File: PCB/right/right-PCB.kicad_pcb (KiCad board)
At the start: 2 copper layers, 171 x 95 mm, 55 parts, among them J1 Modulo-Jack, J2 Modulo-Jack, SW1 SW_Push, SW10 SW_Push, SW11 SW_Push, SW12 SW_Push, SW13 SW_Push, SW14 SW_Push, SW15 SW_Push, SW16 SW_Push, SW17 SW_Push, SW18 SW_Push, SW19 SW_Push, SW2 SW_Push, SW20 SW_Push, SW21 SW_Push, SW22 SW_Push, SW23 SW_Push, SW24 SW_Push, SW25 SW_Push, SW26 SW_Push, SW27 SW_Push, SW28 SW_Push, SW29 SW_Push, SW3 SW_Push, SW30 SW_Push, SW31 SW_Push, SW32 SW_Push, SW33 SW_Push, SW34 SW_Push, SW35 SW_Push, SW36 SW_Push, SW37 SW_Push, SW38 SW_Push, SW4 SW_Push, SW5 SW_Push, SW50 SW_DIP_x04, SW6 SW_Push, SW7 SW_Push, SW8 SW_Push, SW9 SW_Push, U1 MCP23017_SP, U2 MCP23017_SP, U3 MCP23017_SP

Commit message: add sign
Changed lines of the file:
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@@
     (pad "" np_thru_hole circle (at 2.54 -5.08) (size 3 3) (drill 3) (layers *.Cu *.Mask))
   )
-  (gr_text "satsuma JP SMD rev.1          Designed by @ysni_pub" (at 102.235 137.16) (layer B.SilkS)
-    (effects (font (size 2 2) (thickness 0.2)) (justify mirror))
+  (gr_text "satsuma JP SMD rev.1    Designed by @ysni_pub" (at 179.07 137.795) (layer F.SilkS)
+    (effects (font (size 1.5 1.5) (thickness 0.15)))
   )
   (gr_circle (center 71.275 102.15) (end 71.755 104.14) (layer Dwgs.User) (width 0.15))

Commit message: add silk
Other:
- board text added: "1MΩ"
- board text added: "1μF"
- board text added: "A2"
- board text added: "KHS42E"
- board text added: "LED"
- board text added: "MCP23017-E/SO"
- board text added: "OFF"
- board text added: "ON"
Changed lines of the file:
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@@
   (general
     (thickness 1.6)
-    (drawings 25)
+    (drawings 35)
     (tracks 610)
     (zones 0)
@@
     (pad "" np_thru_hole circle (at 2.54 -5.08) (size 3 3) (drill 3) (layers *.Cu *.Mask))
   )
+  (gr_text MCP23017-E/SO (at 166.37 102.235) (layer B.SilkS)
+    (effects (font (size 1 1) (thickness 0.15)) (justify mirror))
+  )
+  (gr_text MCP23017-E/SO (at 161.29 64.135) (layer B.SilkS)
+    (effects (font (size 1 1) (thickness 0.15)) (justify mirror))
+  )
+  (gr_text MCP23017-E/SO (at 109.22 102.235) (layer B.SilkS)
+    (effects (font (size 1 1) (thickness 0.15)) (justify mirror))
+  )
+  (gr_text LED (at 83.185 104.775) (layer F.SilkS)
+    (effects (font (size 1 1) (thickness 0.15)))
+  )
+  (gr_text 1MΩ (at 90.805 66.675) (layer F.SilkS)
+    (effects (font (size 1 1) (thickness 0.15)))
+  )
+  (gr_text 1μF (at 104.775 66.04) (layer B.SilkS)
+    (effects (font (size 1 1) (thickness 0.15)) (justify mirror))
+  )
+  (gr_text A2 (at 76.835 59.055) (layer B.SilkS)
+    (effects (font (size 1 1) (thickness 0.15)) (justify mirror))
+  )
+  (gr_text OFF (at 79.375 68.58) (layer B.SilkS)
+    (effects (font (size 1 1) (thickness 0.15)) (justify mirror))
+  )
+  (gr_text ON (at 78.74 60.96) (layer B.SilkS)
+    (effects (font (size 1 1) (thickness 0.15)) (justify mirror))
+  )
+  (gr_text KHS42E (at 74.93 64.77) (layer B.SilkS)
+    (effects (font (size 1 1) (thickness 0.15)) (justify mirror))
+  )
   (gr_text "satsuma JP SMD rev.1    Designed by @ysni_pub" (at 179.07 137.795) (layer F.SilkS)

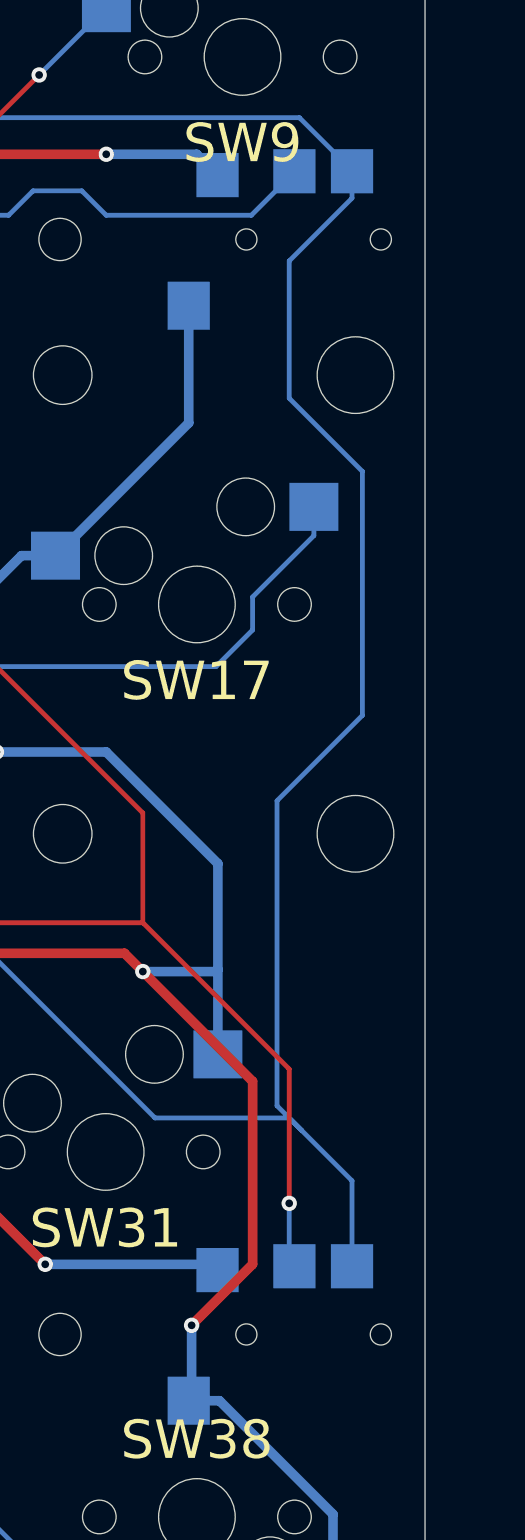
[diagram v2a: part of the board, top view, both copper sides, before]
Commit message: change TRRS jack footprint to PJ-320D
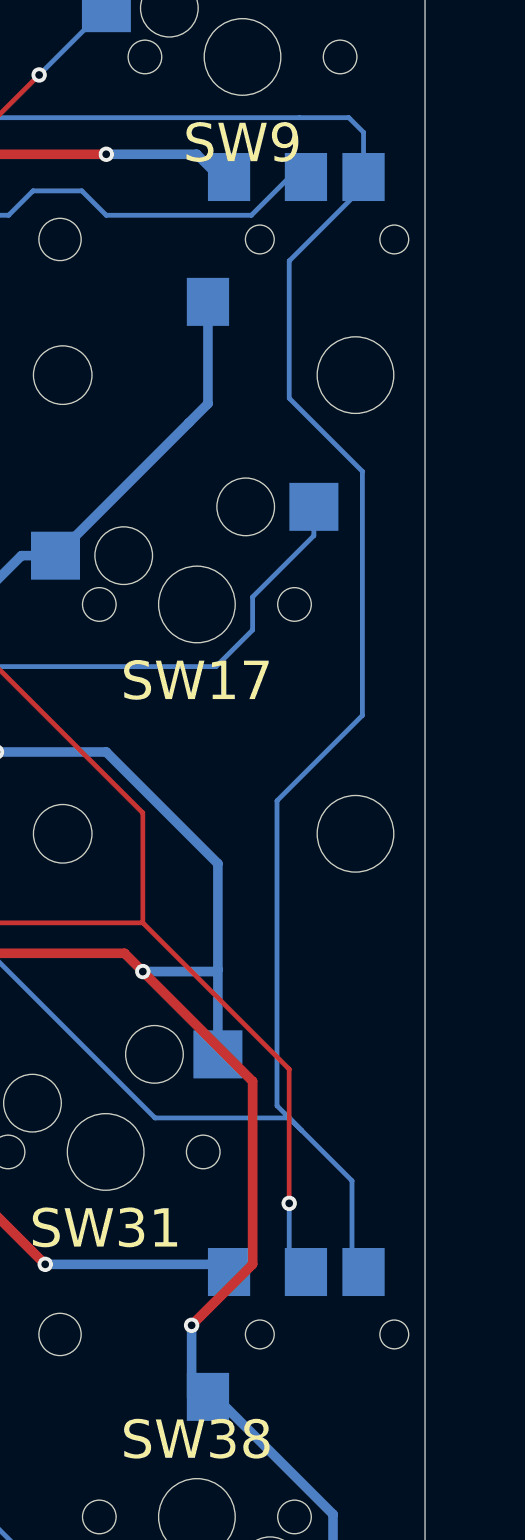
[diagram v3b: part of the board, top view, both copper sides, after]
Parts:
- J1, J2: footprint lib:TRRS_SMD_SJ2-3574A-SMT_ABCD -> lib:PJ-320D
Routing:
- net SDA: track 202.4 -> 204.5 mm
- net GND: track 1055.8 -> 1054.6 mm
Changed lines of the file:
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@@
     (thickness 1.6)
     (drawings 35)
-    (tracks 610)
+    (tracks 611)
     (zones 0)
     (modules 55)
@@
     (add_net VCC)
   )
-  (module lib:satsuma-orange (layer B.Cu)
+  (module lib:PJ-320D (layer B.Cu)
+    (at 209 64.125 180)
+    (fp_text reference J2 (at 6 -6.35) (layer B.SilkS)
+      (effects (font (size 1 1) (thickness 0.15)) (justify mirror))
+    )
+    (fp_text value Modulo-Jack (at 6 6.35) (layer B.Fab)
+      (effects (font (size 1 1) (thickness 0.15)) (justify mirror))
+    )
+    (fp_line (start -2 -2.5) (end 0 -2.5) (layer B.SilkS) (width 0.15))
+    (fp_line (start -2 2.5) (end -2 -2.5) (layer B.SilkS) (width 0.15))
+    (fp_line (start 0 2.5) (end -2 2.5) (layer B.SilkS) (width 0.15))
+    (fp_line (start 0 -3.05) (end 0 3.05) (layer B.SilkS) (width 0.15))
+    (fp_line (start 12.1 -3.05) (end 0 -3.05) (layer B.SilkS) (width 0.15))
+    (fp_line (start 12.1 3.05) (end 12.1 -3.05) (layer B.SilkS) (width 0.15))
+    (fp_line (start 0 3.05) (end 12.1 3.05) (layer B.SilkS) (width 0.15))
+    (pad B smd rect (at 3.2 3.25 180) (size 2.2 2.5) (layers B.Cu B.Paste B.Mask)
+      (net 2 SDA))
+    (pad C smd rect (at 6.2 3.25 180) (size 2.2 2.5) (layers B.Cu B.Paste B.Mask)
+      (net 66 SCL))
+    (pad D smd rect (at 10.2 3.25 180) (size 2.2 2.5) (layers B.Cu B.Paste B.Mask)
+      (net 58 VCC))
+    (pad A smd rect (at 11.3 -3.25 180) (size 2.2 2.5) (layers B.Cu B.Paste B.Mask)
+      (net 1 GND))
+    (pad "" np_thru_hole circle (at 8.6 0 180) (size 1.5 1.5) (drill 1.5) (layers *.Cu *.Mask))
+    (pad "" np_thru_hole circle (at 1.6 0 180) (size 1.5 1.5) (drill 1.5) (layers *.Cu *.Mask))
+  )
+  (module lib:PJ-320D (layer B.Cu)
+    (at 209 121.125 180)
+    (fp_text reference J1 (at 6 -6.35) (layer B.SilkS)
+      (effects (font (size 1 1) (thickness 0.15)) (justify mirror))
+    )
+    (fp_text value Modulo-Jack (at 6 6.35) (layer B.Fab)
+      (effects (font (size 1 1) (thickness 0.15)) (justify mirror))
+    )
+    (fp_line (start -2 -2.5) (end 0 -2.5) (layer B.SilkS) (width 0.15))
+    (fp_line (start -2 2.5) (end -2 -2.5) (layer B.SilkS) (width 0.15))
+    (fp_line (start 0 2.5) (end -2 2.5) (layer B.SilkS) (width 0.15))
+    (fp_line (start 0 -3.05) (end 0 3.05) (layer B.SilkS) (width 0.15))
+    (fp_line (start 12.1 -3.05) (end 0 -3.05) (layer B.SilkS) (width 0.15))
+    (fp_line (start 12.1 3.05) (end 12.1 -3.05) (layer B.SilkS) (width 0.15))
+    (fp_line (start 0 3.05) (end 12.1 3.05) (layer B.SilkS) (width 0.15))
+    (pad B smd rect (at 3.2 3.25 180) (size 2.2 2.5) (layers B.Cu B.Paste B.Mask)
+      (net 2 SDA))
+    (pad C smd rect (at 6.2 3.25 180) (size 2.2 2.5) (layers B.Cu B.Paste B.Mask)
+      (net 66 SCL))
+    (pad D smd rect (at 10.2 3.25 180) (size 2.2 2.5) (layers B.Cu B.Paste B.Mask)
+      (net 58 VCC))
+    (pad A smd rect (at 11.3 -3.25 180) (size 2.2 2.5) (layers B.Cu B.Paste B.Mask)
+      (net 1 GND))
+    (pad "" np_thru_hole circle (at 8.6 0 180) (size 1.5 1.5) (drill 1.5) (layers *.Cu *.Mask))
+    (pad "" np_thru_hole circle (at 1.6 0 180) (size 1.5 1.5) (drill 1.5) (layers *.Cu *.Mask))
+  )
+  (module lib:satsuma-orange locked (layer B.Cu)
     (at 139.7 63.5 180)
     (fp_text reference G*** (at 0 0) (layer B.SilkS) hide
@@
     )
   )
-  (module lib:TRRS_SMD_SJ2-3574A-SMT_ABCD (layer B.Cu)
-    (at 209 64.125 180)
-    (fp_text reference J2 (at 6 -6.35 180) (layer B.SilkS)
-      (effects (font (size 1 1) (thickness 0.15)) (justify mirror))
-    )
-    (fp_text value Modulo-Jack (at 6 6.35 180) (layer B.Fab)
-      (effects (font (size 1 1) (thickness 0.15)) (justify mirror))
-    )
-    (fp_line (start -1.2 -2.8) (end 0 -2.8) (layer B.SilkS) (width 0.15))
-    (fp_line (start -1.2 2.8) (end -1.2 -2.8) (layer B.SilkS) (width 0.15))
-    (fp_line (start 0 2.8) (end -1.2 2.8) (layer B.SilkS) (width 0.15))
-    (fp_line (start 0 -3) (end 0 3) (layer B.SilkS) (width 0.15))
-    (fp_line (start 13.8 -3) (end 0 -3) (layer B.SilkS) (width 0.15))
-    (fp_line (start 13.8 3) (end 13.8 -3) (layer B.SilkS) (width 0.15))
-    (fp_line (start 0 3) (end 13.8 3) (layer B.SilkS) (width 0.15))
-    (pad B smd rect (at 3.8 3.55 180) (size 2.2 2.3) (layers B.Cu B.Paste B.Mask)
-      (net 2 SDA))
-    (pad C smd rect (at 6.8 3.55 180) (size 2.2 2.3) (layers B.Cu B.Paste B.Mask)
-      (net 66 SCL))
-    (pad D smd rect (at 10.8 3.35 180) (size 2.2 2.3) (layers B.Cu B.Paste B.Mask)
-      (net 58 VCC))
-    (pad A smd rect (at 12.3 -3.45 180) (size 2.2 2.5) (layers B.Cu B.Paste B.Mask)
-      (net 1 GND))
-    (pad "" np_thru_hole circle (at 9.3 0 180) (size 1.1 1.1) (drill 1.1) (layers *.Cu *.Mask))
-    (pad "" np_thru_hole circle (at 2.3 0 180) (size 1.1 1.1) (drill 1.1) (layers *.Cu *.Mask))
-  )
-  (module lib:TRRS_SMD_SJ2-3574A-SMT_ABCD (layer B.Cu)
-    (at 209 121.125 180)
-    (fp_text reference J1 (at 6 -6.35) (layer B.SilkS)
-      (effects (font (size 1 1) (thickness 0.15)) (justify mirror))
-    )
-    (fp_text value Modulo-Jack (at 6 6.35) (layer B.Fab)
-      (effects (font (size 1 1) (thickness 0.15)) (justify mirror))
-    )
-    (fp_line (start -1.2 -2.8) (end 0 -2.8) (layer B.SilkS) (width 0.15))
-    (fp_line (start -1.2 2.8) (end -1.2 -2.8) (layer B.SilkS) (width 0.15))
-    (fp_line (start 0 2.8) (end -1.2 2.8) (layer B.SilkS) (width 0.15))
-    (fp_line (start 0 -3) (end 0 3) (layer B.SilkS) (width 0.15))
-    (fp_line (start 13.8 -3) (end 0 -3) (layer B.SilkS) (width 0.15))
-    (fp_line (start 13.8 3) (end 13.8 -3) (layer B.SilkS) (width 0.15))
-    (fp_line (start 0 3) (end 13.8 3) (layer B.SilkS) (width 0.15))
-    (pad B smd rect (at 3.8 3.55 180) (size 2.2 2.3) (layers B.Cu B.Paste B.Mask)
-      (net 2 SDA))
-    (pad C smd rect (at 6.8 3.55 180) (size 2.2 2.3) (layers B.Cu B.Paste B.Mask)
-      (net 66 SCL))
-    (pad D smd rect (at 10.8 3.35 180) (size 2.2 2.3) (layers B.Cu B.Paste B.Mask)
-      (net 58 VCC))
-    (pad A smd rect (at 12.3 -3.45 180) (size 2.2 2.5) (layers B.Cu B.Paste B.Mask)
-      (net 1 GND))
-    (pad "" np_thru_hole circle (at 9.3 0 180) (size 1.1 1.1) (drill 1.1) (layers *.Cu *.Mask))
-    (pad "" np_thru_hole circle (at 2.3 0 180) (size 1.1 1.1) (drill 1.1) (layers *.Cu *.Mask))
-  )
   (module Capacitor_SMD:C_2220_5650Metric_Pad1.97x5.40mm_HandSolder (layer B.Cu)
     (at 104.775 66.04 270)
@@
   (segment (start 204.21 130.485) (end 204.21 133.165) (width 0.5) (layer B.Cu) (net 1) (status 20))
   (segment (start 198.3 124.575) (end 204.21 130.485) (width 0.5) (layer B.Cu) (net 1))
-  (segment (start 196.7 124.575) (end 198.3 124.575) (width 0.5) (layer B.Cu) (net 1) (status 10))
   (segment (start 181.567 125.545) (end 181.592 125.545) (width 0.5) (layer B.Cu) (net 1) (status 30))
   (segment (start 173.335 117.313) (end 181.567 125.545) (width 0.5) (layer B.Cu) (net 1) (status 20))
@@
   (segment (start 181.592 87.545) (end 181.617 87.545) (width 0.5) (layer B.Cu) (net 1) (status 30))
   (segment (start 192.405 90.805) (end 198.217 96.617) (width 0.5) (layer B.Cu) (net 1))
-  (segment (start 196.7 73.675) (end 196.7 67.575) (width 0.5) (layer B.Cu) (net 1) (status 20))
   (segment (start 189.79 80.585) (end 196.7 73.675) (width 0.5) (layer B.Cu) (net 1) (status 10))
   (segment (start 189.765 80.585) (end 189.79 80.585) (width 0.5) (layer B.Cu) (net 1) (status 30))
@@
   (via (at 196.85 120.65) (size 0.8) (drill 0.4) (layers F.Cu B.Cu) (net 1))
   (segment (start 200.025 117.475) (end 196.85 120.65) (width 0.5) (layer F.Cu) (net 1))
-  (segment (start 196.85 124.425) (end 196.7 124.575) (width 0.5) (layer B.Cu) (net 1) (status 30))
   (segment (start 196.85 120.65) (end 196.85 124.425) (width 0.5) (layer B.Cu) (net 1) (status 20))
   (via (at 112.717 121.607) (size 0.8) (drill 0.4) (layers F.Cu B.Cu) (net 1))
@@
   (segment (start 183.515 83.185) (end 183.515 87.63) (width 0.5) (layer F.Cu) (net 1))
   (segment (start 186.69 90.805) (end 192.405 90.805) (width 0.5) (layer B.Cu) (net 1))
+  (segment (start 197.7 72.675) (end 197.7 67.375) (width 0.5) (layer B.Cu) (net 1))
+  (segment (start 196.7 73.675) (end 197.7 72.675) (width 0.5) (layer B.Cu) (net 1))
   (segment (start 182.88 61.595) (end 186.69 57.785) (width 0.25) (layer B.Cu) (net 2))
   (segment (start 205.2 60.525) (end 205.2 60.575) (width 0.25) (layer B.Cu) (net 2) (status 30))
-  (segment (start 202.46 57.785) (end 205.2 60.525) (width 0.25) (layer B.Cu) (net 2) (status 20))
   (segment (start 186.69 57.785) (end 202.46 57.785) (width 0.25) (layer B.Cu) (net 2))
   (segment (start 168.91 60.96) (end 169.545 61.595) (width 0.25) (layer B.Cu) (net 2))
@@
   (segment (start 205.74 76.2) (end 201.93 72.39) (width 0.25) (layer B.Cu) (net 2))
   (segment (start 201.93 72.39) (end 201.93 65.245) (width 0.25) (layer B.Cu) (net 2))
+  (segment (start 205.8 60.875) (end 205.8 58.55) (width 0.25) (layer B.Cu) (net 2))
+  (segment (start 205.035 57.785) (end 202.46 57.785) (width 0.25) (layer B.Cu) (net 2))
+  (segment (start 205.8 58.55) (end 205.035 57.785) (width 0.25) (layer B.Cu) (net 2))
   (segment (start 160.02 60.96) (end 160.02 59.485) (width 0.25) (layer B.Cu) (net 3) (status 20))
   (segment (start 157.48 63.5) (end 160.02 60.96) (width 0.25) (layer B.Cu) (net 3))

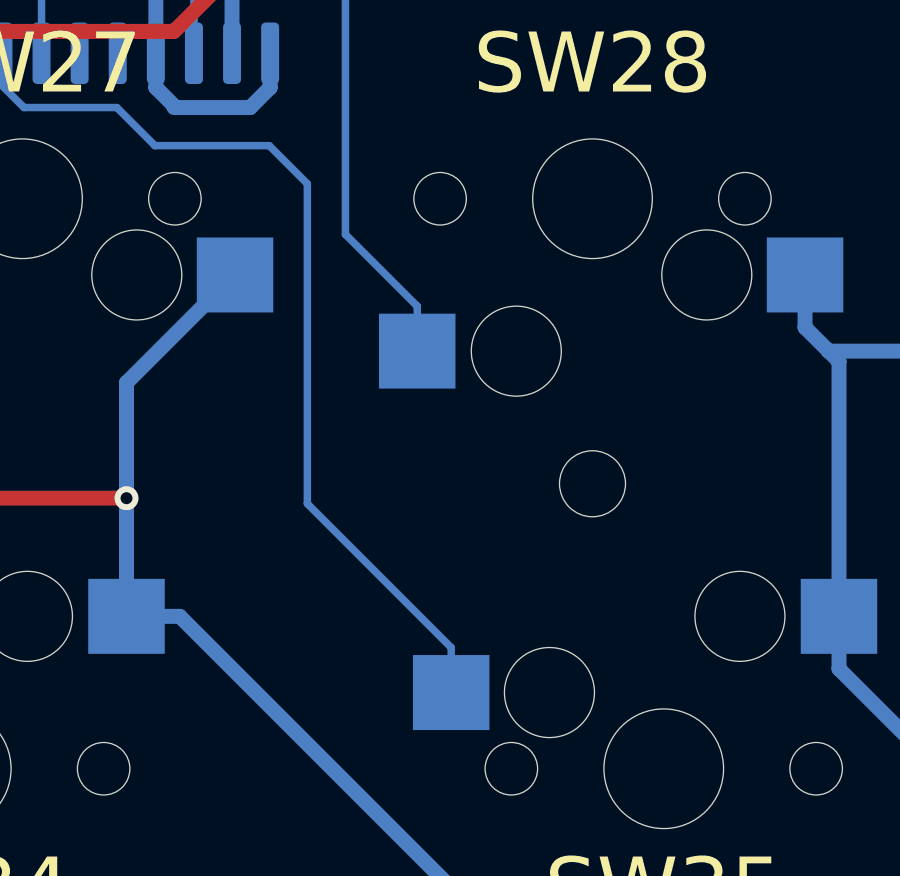
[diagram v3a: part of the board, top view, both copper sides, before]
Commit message: move right drillhole
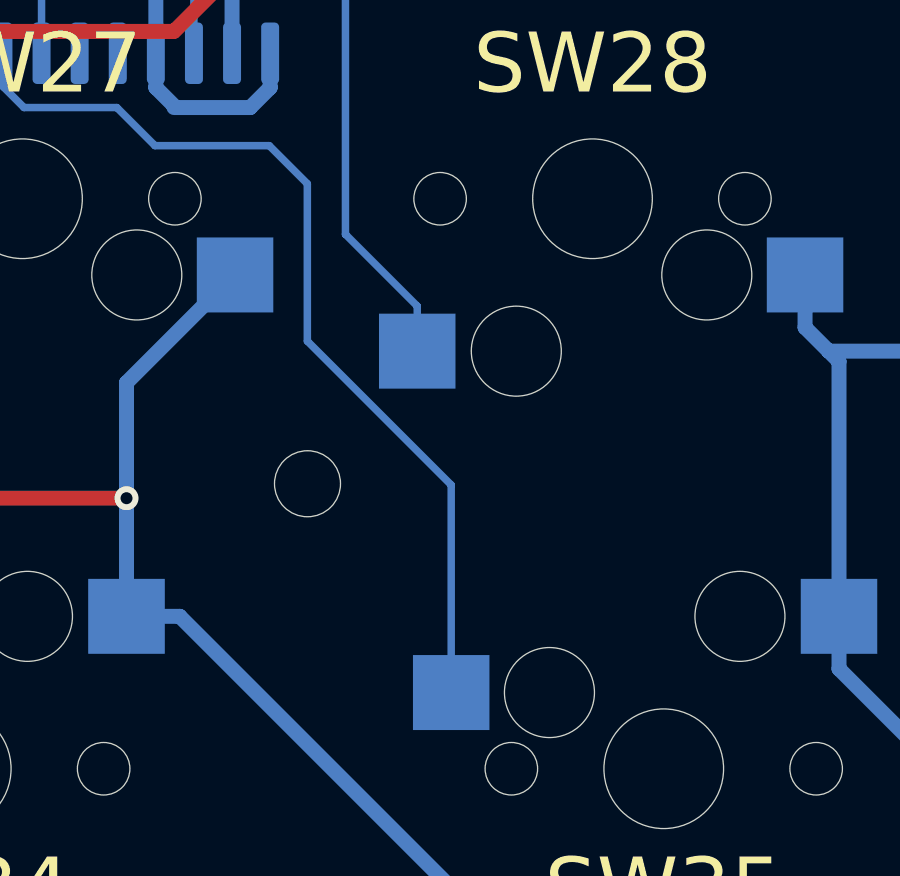
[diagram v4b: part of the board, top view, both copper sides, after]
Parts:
- moved ? 9.50 mm to (118.8, 121.1)
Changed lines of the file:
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@@
   )
   (module lib:MountingHole_2.2mm_M2 locked (layer F.Cu)
-    (at 128.25 121.125)
+    (at 118.75 121.125)
     (descr "Mounting Hole 2.2mm, no annular, M2")
     (tags "mounting hole 2.2mm no annular m2")
@@
   (segment (start 108.615 107.9) (end 109.3 108.585) (width 0.25) (layer B.Cu) (net 36))
   (segment (start 108.615 106.775) (end 108.615 107.9) (width 0.25) (layer B.Cu) (net 36) (status 10))
-  (segment (start 123.54 126.585) (end 123.54 128.085) (width 0.25) (layer B.Cu) (net 36) (status 20))
-  (segment (start 118.745 121.79) (end 123.54 126.585) (width 0.25) (layer B.Cu) (net 36))
-  (segment (start 118.745 111.125) (end 118.745 121.79) (width 0.25) (layer B.Cu) (net 36))
   (segment (start 112.395 108.585) (end 113.665 109.855) (width 0.25) (layer B.Cu) (net 36))
   (segment (start 109.3 108.585) (end 112.395 108.585) (width 0.25) (layer B.Cu) (net 36))
   (segment (start 113.665 109.855) (end 117.475 109.855) (width 0.25) (layer B.Cu) (net 36))
   (segment (start 117.475 109.855) (end 118.745 111.125) (width 0.25) (layer B.Cu) (net 36))
+  (segment (start 123.54 128.085) (end 123.54 121.165) (width 0.25) (layer B.Cu) (net 36))
+  (segment (start 123.54 121.165) (end 118.745 116.37) (width 0.25) (layer B.Cu) (net 36))
+  (segment (start 118.745 111.125) (end 118.745 116.37) (width 0.25) (layer B.Cu) (net 36))
   (segment (start 159.265 109.975) (end 159.265 106.775) (width 0.25) (layer B.Cu) (net 37) (status 20))
   (segment (start 156.845 112.395) (end 159.265 109.975) (width 0.25) (layer B.Cu) (net 37))

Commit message: move screw holl
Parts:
- moved ? 4.75 mm to (185.2, 121.1)
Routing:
- net SW38: track 45.8 -> 48.8 mm
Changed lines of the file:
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@@
     (thickness 1.6)
     (drawings 35)
-    (tracks 611)
+    (tracks 613)
     (zones 0)
     (modules 55)
@@
   )
   (module lib:MountingHole_2.2mm_M2 locked (layer F.Cu)
-    (at 190 121.125)
+    (at 185.25 121.125)
     (descr "Mounting Hole 2.2mm, no annular, M2")
     (tags "mounting hole 2.2mm no annular m2")
@@
   (segment (start 163.075 108.465) (end 163.71 109.1) (width 0.25) (layer B.Cu) (net 39))
   (segment (start 163.71 109.1) (end 172.6 109.1) (width 0.25) (layer B.Cu) (net 39))
-  (segment (start 172.6 109.1) (end 186.69 123.19) (width 0.25) (layer B.Cu) (net 39))
-  (segment (start 186.69 123.19) (end 186.69 131.137) (width 0.25) (layer B.Cu) (net 39))
-  (segment (start 186.69 131.137) (end 191.258 135.705) (width 0.25) (layer B.Cu) (net 39) (status 20))
+  (segment (start 189.0665 133.5135) (end 189.0665 120.4865) (width 0.25) (layer B.Cu) (net 39))
+  (segment (start 189.0665 133.5135) (end 191.258 135.705) (width 0.25) (layer B.Cu) (net 39))
+  (segment (start 183.515 114.935) (end 178.435 114.935) (width 0.25) (layer B.Cu) (net 39))
+  (segment (start 189.0665 120.4865) (end 183.515 114.935) (width 0.25) (layer B.Cu) (net 39))
+  (segment (start 172.6 109.1) (end 178.435 114.935) (width 0.25) (layer B.Cu) (net 39))
   (via (at 167.64 66.675) (size 0.8) (drill 0.4) (layers F.Cu B.Cu) (net 40))
   (segment (start 167.64 68.785) (end 167.64 66.675) (width 0.25) (layer B.Cu) (net 40) (status 10))
